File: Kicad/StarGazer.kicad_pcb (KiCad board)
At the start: 4 copper layers, 94 parts, among them J201 USB_B_Micro, J202 Conn_02x01 BATTERY, J301 GPS - I2C OUT, J302 SCREEN - I2C OUT, J303 SWD_DEBUG, J304 CONN_JOYSTICK, J305 GENERAL - I2C OUT, SW201 SW_DIP_x01, SW301 RESET PUSH, U101 STM32F070F6Px, U201 STBC08, U202 AP22811BW5, U203 TLV75528PDBV, U301 TSX-3225, U302 MMC5603NJ, U303 LSM6DS33TR, U304 74HC595PW, U305 74HC595PW, U306 74HC595PW

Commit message: End of night, progress continues.
Parts are getting initial placement.

confidence raises.
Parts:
- J301: value GPS - I2C OUT -> I2C_CONNECTOR_OUT
- J302: value SCREEN - I2C OUT -> I2C_CONNECTOR_OUT
- J305: value GENERAL - I2C OUT -> I2C_CONNECTOR_OUT
- moved C204 255.0 mm to (252.4, -119.0), turned to 180 degrees
- moved R301 250.2 mm to (138.1, -120.3), turned to 180 degrees
- moved C203 249.4 mm to (243.3, -119.0)
- moved U203 246.7 mm to (248.0, -118.4)
- moved SW301 239.7 mm to (146.6, -120.3)
- moved R201 239.6 mm to (214.1, -117.1), turned to 180 degrees
- moved U201 238.4 mm to (208.4, -116.7)
- moved J202 236.8 mm to (203.1, -126.0)
- moved C201 234.4 mm to (192.9, -117.5), turned to 270 degrees
- moved R203 232.8 mm to (197.1, -114.6)
- moved D202 232.7 mm to (202.3, -114.6), turned to 180 degrees
- moved C302 232.1 mm to (142.7, -115.4), turned to 270 degrees
- moved R202 230.2 mm to (197.1, -118.4)
- moved D201 230.2 mm to (202.3, -118.4), turned to 180 degrees
- moved J201 229.2 mm to (204.7, -103.9)
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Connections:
- J201 pad 2: Net-(J201-Pad2) -> (no net)
- J201 pad 3: Net-(J201-Pad3) -> (no net)
- J201 pad 4: Net-(J201-Pad4) -> (no net)
- RV301 pad 1: Net-(RV301-Pad1) -> (no net)
- U202 pad 3: Net-(U202-Pad3) -> (no net)
- U203 pad 4: Net-(U203-Pad4) -> (no net)
- U301 pad 2: (no net) -> GND
- U303 pad 14: Net-(U303-Pad14) -> (no net)
- U306 pad 9: Net-(U306-Pad9) -> (no net)
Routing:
- net GND: track 0.00 -> 34.4 mm, vias 0 -> 18
- net V_REG: track 19.4 -> 33.1 mm, vias 0 -> 4
- net Net-(C303-Pad1): track 0.00 -> 8.31 mm
- net V_USB: track 0.00 -> 8.18 mm
- net Net-(R204-Pad1): track 0.00 -> 7.25 mm
- net SW_3_3V: track 0.00 -> 6.61 mm
- net Net-(D201-Pad1): track 0.00 -> 4.38 mm
- net Net-(D202-Pad1): track 0.00 -> 3.81 mm
- net OSC_IN: track 0.00 -> 3.60 mm
- net Net-(C202-Pad1): track 0.00 -> 3.38 mm
- net Net-(R201-Pad2): track 0.00 -> 3.06 mm
- net Net-(D202-Pad2): track 0.00 -> 2.28 mm
- net Net-(D201-Pad2): track 0.00 -> 2.28 mm
- added copper zone on In1.Cu, net GND
- added copper zone on In2.Cu, net V_REG

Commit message: Switching magnometer with an updated part. This change is due to the limitations of JLCPCB's ball grid array.  The ball diameter is 0.25mm, while the component has 0.2 While this could probably be worked around I have never been happy with the part due to it's size and difficulty verifying it would work.
It is twice the cost of the orignal part and requires more support components, but is otherwhys an upgrade.
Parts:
- moved R301 167.0 mm to (201.6, 34.2)
- moved SW301 167.0 mm to (210.1, 34.2)
- moved C202 166.9 mm to (185.3, 31.0)
- moved R204 166.9 mm to (189.1, 36.5)
- moved R205 166.9 mm to (185.3, 36.5)
- moved SW201 166.9 mm to (180.8, 22.4)
- moved U202 166.9 mm to (180.4, 33.5)
- moved C302 166.1 mm to (206.2, 38.1)
- moved D201 148.6 mm to (235.8, 26.4)
- moved D202 148.6 mm to (235.8, 30.2)
- moved C201 148.6 mm to (226.4, 27.3)
- moved J201 148.6 mm to (238.2, 40.9)
- moved J202 148.6 mm to (236.6, 18.8)
- moved R201 148.6 mm to (247.6, 27.7)
- moved R202 148.6 mm to (230.7, 26.4)
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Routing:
- net V_REG: track 33.1 -> 44.8 mm, vias 4 -> 7
- net GND: track 34.4 -> 41.8 mm, vias 18 -> 21
- net RESET_N: track 0.00 -> 6.08 mm
- net I2C_SCL: track 0.00 -> 4.04 mm
- net I2C_SDA: track 0.00 -> 3.88 mm

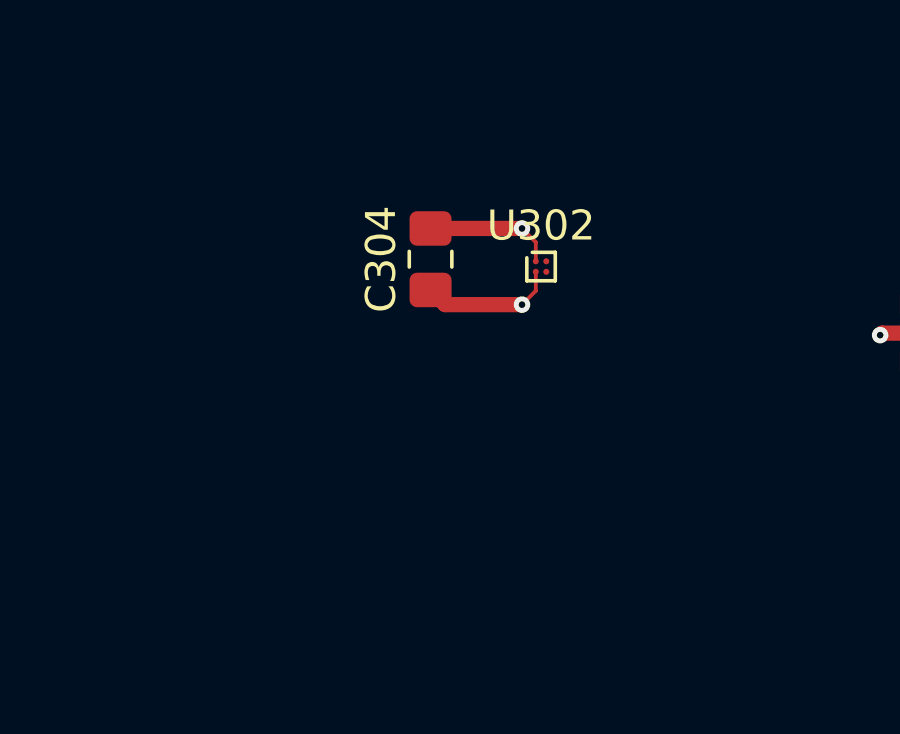
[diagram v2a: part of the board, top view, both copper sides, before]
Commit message: Updated magnometer to LIS3MDL which has a more sane footprint.
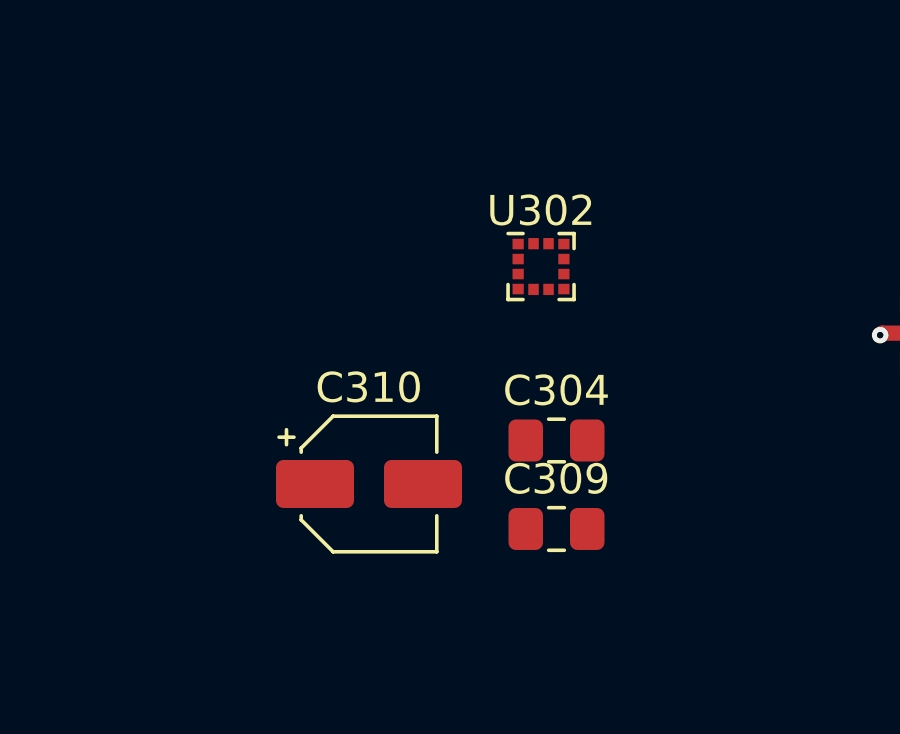
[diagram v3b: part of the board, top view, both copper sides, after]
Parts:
- added C309: 100nF, Capacitor_SMD:C_0805_2012Metric_Pad1.15x1.40mm_HandSolder, F.Cu at (166.2, 40.0)
- added C310: 1uF, Capacitor_SMD:CP_Elec_4x3, F.Cu at (160.0, 38.5)
- C304: value 2.2uF -> 100nF
- U302: value MMC5603NJ -> LIS3MDLTR; footprint Package_BGA:WLP-4_0.73x0.73mm_Layout2x2_P0.35mm_Ball0.22mm_Pad0.2mm_NSMD -> Package_LGA:LGA-12_2x2mm_P0.5mm
- moved C304 7.36 mm to (166.2, 37.0), turned to 0 degrees
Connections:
- C304 pad 1: V_REG -> GND
- C304 pad 2: GND -> Net-(C304-Pad2)
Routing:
- net V_REG: track 44.8 -> 40.3 mm, vias 7 -> 6
- net GND: track 41.8 -> 37.5 mm, vias 21 -> 20

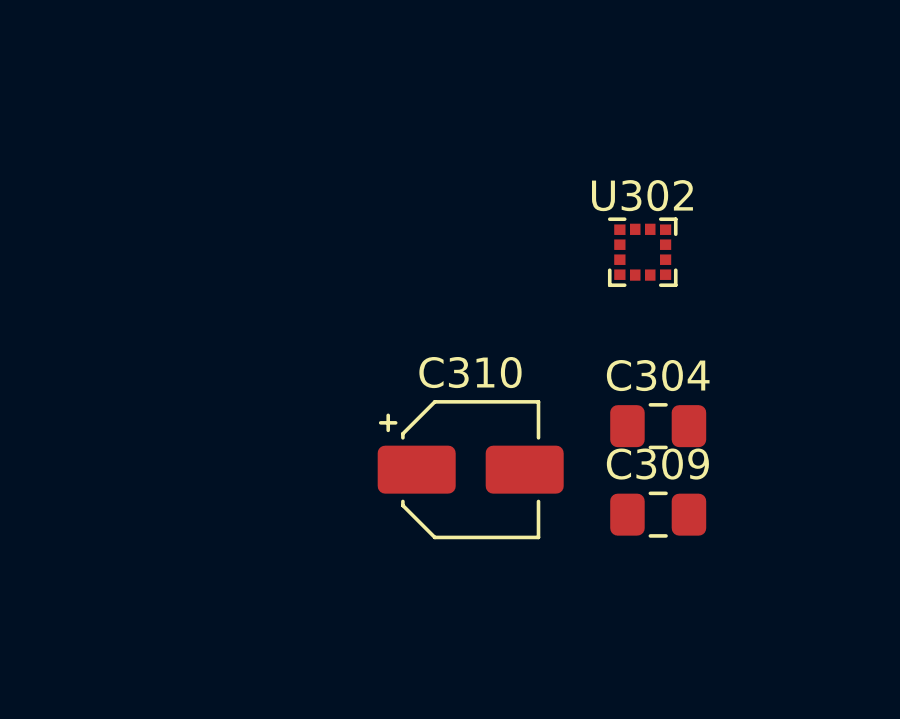
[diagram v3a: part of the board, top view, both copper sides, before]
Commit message: Discovered small bug with BoM script.  It does not acccount for all parameters, such as foot print.  This resulted in it thinking a electro-cap could be a ceramic-cap since they shared the same value.
To simplify parts, C310 is now a ceramic cap at the same value.
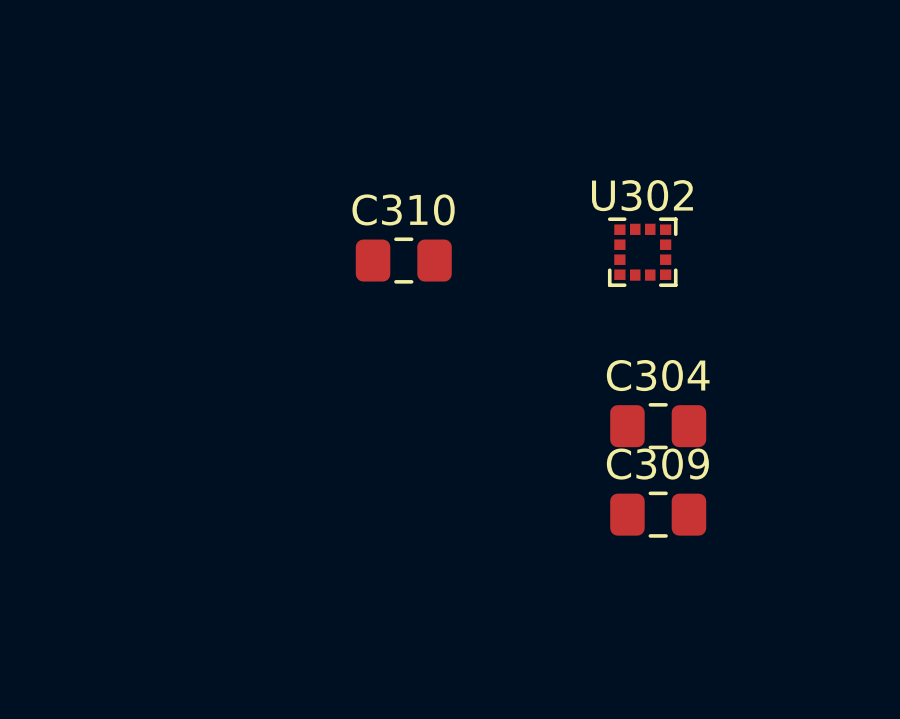
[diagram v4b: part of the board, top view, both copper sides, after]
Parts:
- C310: footprint Capacitor_SMD:CP_Elec_4x3 -> Capacitor_SMD:C_0805_2012Metric_Pad1.15x1.40mm_HandSolder
- moved C310 7.32 mm to (157.8, 31.5)
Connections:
- C310 pad 1: V_REG -> GND
- C310 pad 2: GND -> V_REG
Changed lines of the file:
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@@
     (add_net V_USB)
+  )
+  (module Capacitor_SMD:C_0805_2012Metric_Pad1.15x1.40mm_HandSolder (layer Front)
+    (at 157.77 31.52)
+    (descr "Capacitor SMD 0805 (2012 Metric), square (rectangular) end terminal, IPC_7351 nominal with elongated pad for handsoldering. (Body size source: https://docs.google.com/spreadsheets/d/1BsfQQcO9C6DZCsRaXUlFlo91Tg2WpOkGARC1WS5S8t0/edit?usp=sharing), generated with kicad-footprint-generator")
+    (tags "capacitor handsolder")
+    (attr smd)
+    (fp_text reference C310 (at 0 -1.65) (layer F.SilkS)
+      (effects (font (size 1 1) (thickness 0.15)))
+    )
+    (fp_text value 1uF (at 0 1.65) (layer F.Fab)
+      (effects (font (size 1 1) (thickness 0.15)))
+    )
+    (fp_text user %R (at 0 0) (layer F.Fab)
+      (effects (font (size 0.5 0.5) (thickness 0.08)))
+    )
+    (fp_line (start 1.85 0.95) (end -1.85 0.95) (layer F.CrtYd) (width 0.05))
+    (fp_line (start 1.85 -0.95) (end 1.85 0.95) (layer F.CrtYd) (width 0.05))
+    (fp_line (start -1.85 -0.95) (end 1.85 -0.95) (layer F.CrtYd) (width 0.05))
+    (fp_line (start -1.85 0.95) (end -1.85 -0.95) (layer F.CrtYd) (width 0.05))
+    (fp_line (start -0.261252 0.71) (end 0.261252 0.71) (layer F.SilkS) (width 0.12))
+    (fp_line (start -0.261252 -0.71) (end 0.261252 -0.71) (layer F.SilkS) (width 0.12))
+    (fp_line (start 1 0.6) (end -1 0.6) (layer F.Fab) (width 0.1))
+    (fp_line (start 1 -0.6) (end 1 0.6) (layer F.Fab) (width 0.1))
+    (fp_line (start -1 -0.6) (end 1 -0.6) (layer F.Fab) (width 0.1))
+    (fp_line (start -1 0.6) (end -1 -0.6) (layer F.Fab) (width 0.1))
+    (pad 2 smd roundrect (at 1.025 0) (size 1.15 1.4) (layers Front F.Paste F.Mask) (roundrect_rratio 0.217391)
+      (net 2 V_REG))
+    (pad 1 smd roundrect (at -1.025 0) (size 1.15 1.4) (layers Front F.Paste F.Mask) (roundrect_rratio 0.217391)
+      (net 1 GND))
+    (model ${KISYS3DMOD}/Capacitor_SMD.3dshapes/C_0805_2012Metric.wrl
+      (at (xyz 0 0 0))
+      (scale (xyz 1 1 1))
+      (rotate (xyz 0 0 0))
+    )
   )
   (module Package_LGA:LGA-12_2x2mm_P0.5mm (layer Front)
@@
       (at (xyz 0 0 0))
       (scale (xyz 1 1 1))
-      (rotate (xyz 0 0 0))
-    )
-  )
-  (module Capacitor_SMD:CP_Elec_4x3 (layer Front)
-    (at 160 38.49)
-    (descr "SMD capacitor, aluminum electrolytic, Nichicon, 4.0x3mm")
-    (tags "capacitor electrolytic")
-    (attr smd)
-    (fp_text reference C310 (at 0 -3.2) (layer F.SilkS)
-      (effects (font (size 1 1) (thickness 0.15)))
-    )
-    (fp_text value 1uF (at 0 3.2) (layer F.Fab)
-      (effects (font (size 1 1) (thickness 0.15)))
-    )
-    (fp_text user %R (at 0 0) (layer F.Fab)
-      (effects (font (size 0.8 0.8) (thickness 0.12)))
-    )
-    (fp_line (start -3.35 1.05) (end -2.4 1.05) (layer F.CrtYd) (width 0.05))
-    (fp_line (start -3.35 -1.05) (end -3.35 1.05) (layer F.CrtYd) (width 0.05))
-    (fp_line (start -2.4 -1.05) (end -3.35 -1.05) (layer F.CrtYd) (width 0.05))
-    (fp_line (start -2.4 1.05) (end -2.4 1.25) (layer F.CrtYd) (width 0.05))
-    (fp_line (start -2.4 -1.25) (end -2.4 -1.05) (layer F.CrtYd) (width 0.05))
-    (fp_line (start -2.4 -1.25) (end -1.25 -2.4) (layer F.CrtYd) (width 0.05))
-    (fp_line (start -2.4 1.25) (end -1.25 2.4) (layer F.CrtYd) (width 0.05))
-    (fp_line (start -1.25 -2.4) (end 2.4 -2.4) (layer F.CrtYd) (width 0.05))
-    (fp_line (start -1.25 2.4) (end 2.4 2.4) (layer F.CrtYd) (width 0.05))
-    (fp_line (start 2.4 1.05) (end 2.4 2.4) (layer F.CrtYd) (width 0.05))
-    (fp_line (start 3.35 1.05) (end 2.4 1.05) (layer F.CrtYd) (width 0.05))
-    (fp_line (start 3.35 -1.05) (end 3.35 1.05) (layer F.CrtYd) (width 0.05))
-    (fp_line (start 2.4 -1.05) (end 3.35 -1.05) (layer F.CrtYd) (width 0.05))
-    (fp_line (start 2.4 -2.4) (end 2.4 -1.05) (layer F.CrtYd) (width 0.05))
-    (fp_line (start -2.75 -1.81) (end -2.75 -1.31) (layer F.SilkS) (width 0.12))
-    (fp_line (start -3 -1.56) (end -2.5 -1.56) (layer F.SilkS) (width 0.12))
-    (fp_line (start -2.26 1.195563) (end -1.195563 2.26) (layer F.SilkS) (width 0.12))
-    (fp_line (start -2.26 -1.195563) (end -1.195563 -2.26) (layer F.SilkS) (width 0.12))
-    (fp_line (start -2.26 -1.195563) (end -2.26 -1.06) (layer F.SilkS) (width 0.12))
-    (fp_line (start -2.26 1.195563) (end -2.26 1.06) (layer F.SilkS) (width 0.12))
-    (fp_line (start -1.195563 2.26) (end 2.26 2.26) (layer F.SilkS) (width 0.12))
-    (fp_line (start -1.195563 -2.26) (end 2.26 -2.26) (layer F.SilkS) (width 0.12))
-    (fp_line (start 2.26 -2.26) (end 2.26 -1.06) (layer F.SilkS) (width 0.12))
-    (fp_line (start 2.26 2.26) (end 2.26 1.06) (layer F.SilkS) (width 0.12))
-    (fp_line (start -1.374773 -1.2) (end -1.374773 -0.8) (layer F.Fab) (width 0.1))
-    (fp_line (start -1.574773 -1) (end -1.174773 -1) (layer F.Fab) (width 0.1))
-    (fp_line (start -2.15 1.15) (end -1.15 2.15) (layer F.Fab) (width 0.1))
-    (fp_line (start -2.15 -1.15) (end -1.15 -2.15) (layer F.Fab) (width 0.1))
-    (fp_line (start -2.15 -1.15) (end -2.15 1.15) (layer F.Fab) (width 0.1))
-    (fp_line (start -1.15 2.15) (end 2.15 2.15) (layer F.Fab) (width 0.1))
-    (fp_line (start -1.15 -2.15) (end 2.15 -2.15) (layer F.Fab) (width 0.1))
-    (fp_line (start 2.15 -2.15) (end 2.15 2.15) (layer F.Fab) (width 0.1))
-    (fp_circle (center 0 0) (end 2 0) (layer F.Fab) (width 0.1))
-    (pad 2 smd roundrect (at 1.8 0) (size 2.6 1.6) (layers Front F.Paste F.Mask) (roundrect_rratio 0.15625)
-      (net 1 GND))
-    (pad 1 smd roundrect (at -1.8 0) (size 2.6 1.6) (layers Front F.Paste F.Mask) (roundrect_rratio 0.15625)
-      (net 2 V_REG))
-    (model ${KISYS3DMOD}/Capacitor_SMD.3dshapes/CP_Elec_4x3.wrl
-      (at (xyz 0 0 0))
-      (scale (xyz 1 1 1))

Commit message: Preparing to begin placing parts on actual PCB
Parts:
- moved C310 371.3 mm to (474.5, -162.3), turned to 180 degrees
- moved C309 362.2 mm to (470.0, -157.2), turned to 90 degrees
- moved C204 360.7 mm to (578.6, -165.4)
- moved J302 360.4 mm to (525.3, -132.1)
- moved U202 360.4 mm to (485.2, -158.8)
- moved C101 360.4 mm to (431.4, -114.2)
- moved C102 360.4 mm to (431.8, -108.5)
- moved C202 360.4 mm to (490.1, -161.3)
- moved C301 360.4 mm to (421.9, -90.2)
- moved C302 360.4 mm to (511.0, -154.2)
- moved C303 360.4 mm to (433.3, -92.7)
- moved C305 360.4 mm to (546.6, -106.2)
- moved R101 360.4 mm to (412.5, -111.6)
- moved R201 360.4 mm to (552.4, -164.6)
- moved R204 360.4 mm to (493.9, -155.7)
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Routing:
- net GND: track 37.5 -> 48.3 mm, vias 20 -> 24
- net V_REG: track 40.3 -> 49.8 mm, vias 6 -> 8
- net Net-(C304-Pad2): track 0.00 -> 2.79 mm
- net V_USB: track 8.18 -> 7.12 mm

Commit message: Center LED ring laid out and connected. Other components will begin to be fitted into place. Silk screen has not been touched.
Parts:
- moved C101 299.9 mm to (145.9, -22.2)
- moved C202 299.9 mm to (204.6, -69.3)
- moved C204 299.9 mm to (293.1, -73.4)
- moved C301 299.9 mm to (136.4, 1.78)
- moved C302 299.9 mm to (225.6, -62.2)
- moved C304 299.9 mm to (180.3, -67.6)
- moved C305 299.9 mm to (261.1, -14.2)
- moved C309 299.9 mm to (184.5, -65.3)
- moved C310 299.9 mm to (189.0, -70.4)
- moved J201 299.9 mm to (257.5, -59.4)
- moved J301 299.9 mm to (221.4, -40.1)
- moved J302 299.9 mm to (239.8, -40.1)
- moved J303 299.9 mm to (172.8, -39.4)
- moved R101 299.9 mm to (127.0, -19.7)
- moved R102 299.9 mm to (125.8, -12.1)
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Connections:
- U101 pad 6: SHIFT_REG_RESET_N -> UI_JOY_X
- U101 pad 7: UI_JOY_X -> UI_JOY_Y
- U101 pad 8: UI_JOY_Y -> SHIFT_REG_OUTPUT_ENABLE_N
- U304 pad 10: SHIFT_REG_RESET_N -> RESET_N
- U304 pad 13: GND -> SHIFT_REG_OUTPUT_ENABLE_N
- U305 pad 10: SHIFT_REG_RESET_N -> RESET_N
- U305 pad 13: GND -> SHIFT_REG_OUTPUT_ENABLE_N
- U306 pad 10: SHIFT_REG_RESET_N -> RESET_N
- U306 pad 13: GND -> SHIFT_REG_OUTPUT_ENABLE_N
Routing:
- net Net-(U304-Pad9): track 0.00 -> 96.4 mm, vias 0 -> 2
- net Net-(U305-Pad9): track 0.00 -> 95.9 mm, vias 0 -> 2
- net GND: track 48.3 -> 111.2 mm, vias 24 -> 54
- net Net-(R312-Pad2): track 0.00 -> 40.6 mm, vias 0 -> 2
- net Net-(R304-Pad2): track 0.00 -> 40.4 mm, vias 0 -> 2
- net Net-(R320-Pad2): track 0.00 -> 39.4 mm, vias 0 -> 2
- net Net-(R327-Pad2): track 0.00 -> 38.5 mm, vias 0 -> 2
- net Net-(R311-Pad2): track 0.00 -> 36.6 mm, vias 0 -> 2
- net Net-(R319-Pad2): track 0.00 -> 35.6 mm, vias 0 -> 2
- net Net-(R326-Pad2): track 0.00 -> 29.9 mm, vias 0 -> 2
- net Net-(R310-Pad2): track 0.00 -> 28.3 mm, vias 0 -> 2
- net Net-(R318-Pad2): track 0.00 -> 27.7 mm, vias 0 -> 2
- net Net-(R313-Pad2): track 0.00 -> 24.7 mm, vias 0 -> 2
- net Net-(R305-Pad2): track 0.00 -> 22.7 mm, vias 0 -> 2
- net Net-(R321-Pad2): track 0.00 -> 22.1 mm, vias 0 -> 2
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
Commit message: Many parts are now placed on PCB.
Work left off on MC, gyro, and mag.

Discovered free-angle mode for traces, which will make connections look better in the future.
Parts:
- removed J305: I2C_CONNECTOR_OUT, Connector_JST:JST_EH_B4B-EH-A_1x04_P2.50mm_Vertical
- moved C201 228.4 mm to (104.9, 106.4)
- moved R202 227.9 mm to (108.7, 104.9), turned to 90 degrees
- moved R201 227.2 mm to (108.0, 89.7), turned to 0 degrees
- moved D201 227.1 mm to (108.7, 99.7), turned to 270 degrees
- moved U201 224.5 mm to (109.9, 93.6), turned to 90 degrees
- moved R203 222.8 mm to (112.0, 104.9), turned to 90 degrees
- moved J202 222.6 mm to (105.6, 82.6), turned to 67.5 degrees
- moved D202 222.1 mm to (112.0, 99.7), turned to 270 degrees
- moved J201 222.0 mm to (103.1, 100.1), turned to 270 degrees
- moved C203 216.6 mm to (122.1, 70.9), turned to 37.5 degrees
- moved C204 215.3 mm to (129.2, 66.3), turned to 127.5 degrees
- moved U203 215.0 mm to (126.2, 68.5), turned to 37.5 degrees
- moved J302 212.8 mm to (126.5, 140.0), turned to 60 degrees
- moved R303 194.8 mm to (167.5, 141.1), turned to 30 degrees
- moved R302 193.6 mm to (166.0, 138.4), turned to 30 degrees
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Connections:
- SW201 pad 1: V_BATT -> Net-(C202-Pad1)
- SW201 pad 2: Net-(C202-Pad1) -> V_BATT
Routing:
- net SW_3_3V: track 6.61 -> 69.2 mm, vias 0 -> 1
- net RESET_N: track 11.6 -> 63.3 mm, vias 3 -> 5
- net SWDIO: track 0.00 -> 47.1 mm
- net SWCLK: track 0.00 -> 44.5 mm
- net GND: track 111.2 -> 149.8 mm
- net V_USB: track 7.12 -> 32.1 mm
- net OSC_OUT: track 0.00 -> 19.3 mm
- net OSC_IN: track 3.60 -> 18.9 mm
- net V_REG: track 44.0 -> 55.5 mm, vias 11 -> 14
- net Net-(C202-Pad1): track 3.38 -> 14.6 mm
- net Net-(U305-Pad9): track 95.9 -> 100.7 mm
- net Net-(R101-Pad2): track 0.00 -> 3.01 mm
- net Net-(R102-Pad2): track 0.00 -> 3.00 mm
- net Net-(C303-Pad1): track 8.31 -> 11.1 mm
- net V_BATT: track 0.00 -> 1.30 mm, vias 0 -> 1
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- added copper zone on In2.Cu, net V_BATT
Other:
- board outline added: 100 x 100 mm

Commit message: All parts on board and routed.  Beginning final part compatibility check.  Big TODO is select GPS, verify parts, and begin route-polish step.
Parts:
- moved C310 242.6 mm to (13.6, 38.6), turned to 292.5 degrees
- moved C309 235.5 mm to (16.0, 37.6), turned to 292.5 degrees
- moved U302 234.7 mm to (17.3, 41.1), turned to 202.5 degrees
- moved C304 228.8 mm to (18.5, 36.6), turned to 292.5 degrees
- moved U303 192.9 mm to (39.1, 2.41), turned to 270 degrees
- moved C305 187.6 mm to (40.6, -1.79), turned to 270 degrees
- moved C306 181.1 mm to (-7.37, -41.6)
- moved C101 180.3 mm to (42.0, -10.2)
- moved C301 180.3 mm to (32.5, -31.7)
- moved D322 180.3 mm to (22.5, 22.5)
- moved C102 180.3 mm to (36.9, -22.9)
- moved C201 180.3 mm to (-45.1, 6.41)
- moved C202 180.3 mm to (-32.3, -15.9)
- moved C203 180.3 mm to (-27.9, -29.2)
- moved C204 180.3 mm to (-20.8, -33.8)
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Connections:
- J301 pad 2: I2C_SCL -> I2C_SDA
- J301 pad 3: I2C_SDA -> I2C_SCL
- J302 pad 2: I2C_SCL -> I2C_SDA
- J302 pad 3: I2C_SDA -> I2C_SCL
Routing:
- net SHIFT_REG_LATCH: track 0.00 -> 229.7 mm, vias 0 -> 4
- net SHIFT_REG_OUTPUT_ENABLE_N: track 0.00 -> 229.7 mm, vias 0 -> 4
- net SHIFT_REG_CLK: track 0.00 -> 226.7 mm, vias 0 -> 4
- net RESET_N: track 63.3 -> 247.0 mm
- net I2C_SCL: track 4.04 -> 128.7 mm
- net I2C_SDA: track 3.88 -> 126.8 mm
- net SHIFT_REG_DATA_IN: track 0.00 -> 58.4 mm, vias 0 -> 2
- net UI_JOY_Y: track 0.00 -> 31.8 mm, vias 0 -> 1
- net UI_JOY_X: track 0.00 -> 26.7 mm, vias 0 -> 1
- net UI_BUTTON: track 0.00 -> 14.5 mm, vias 0 -> 1
- net SWDIO: track 47.1 -> 52.6 mm, vias 0 -> 1
- net SWCLK: track 44.5 -> 48.7 mm, vias 0 -> 1
- net Net-(U305-Pad9): track 100.7 -> 97.9 mm
- net OSC_OUT: track 19.3 -> 20.8 mm
- net Net-(U304-Pad9): track 96.1 -> 97.6 mm
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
